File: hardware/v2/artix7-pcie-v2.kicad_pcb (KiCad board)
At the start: 4 copper layers, 60 x 51 mm, 187 parts, among them J1 Conn_02x20_Odd_Even, J10 USB_B_Micro, J2 Conn_02x20_Odd_Even, J4 USB3_A, J5 USB3_A_AS_PCIE, J6 JTAG, J7 Conn_01x02, J8 SER, SW1 PROG, SW2 USER, U1 XC7A75T-FGG484, U10 TPS74701DRCR, U2 MX25L51245GZ2I-10G, U3 TLV62569DBVR, U4 5P49V6965A000NLGI, U5 TLV62569PDDCR, U6 TLV62569DBVR, U7 TLV62569DBVR, U8 TLV62569DBVR, U9 TPS74701DRCR, X1 25MHz/10pF

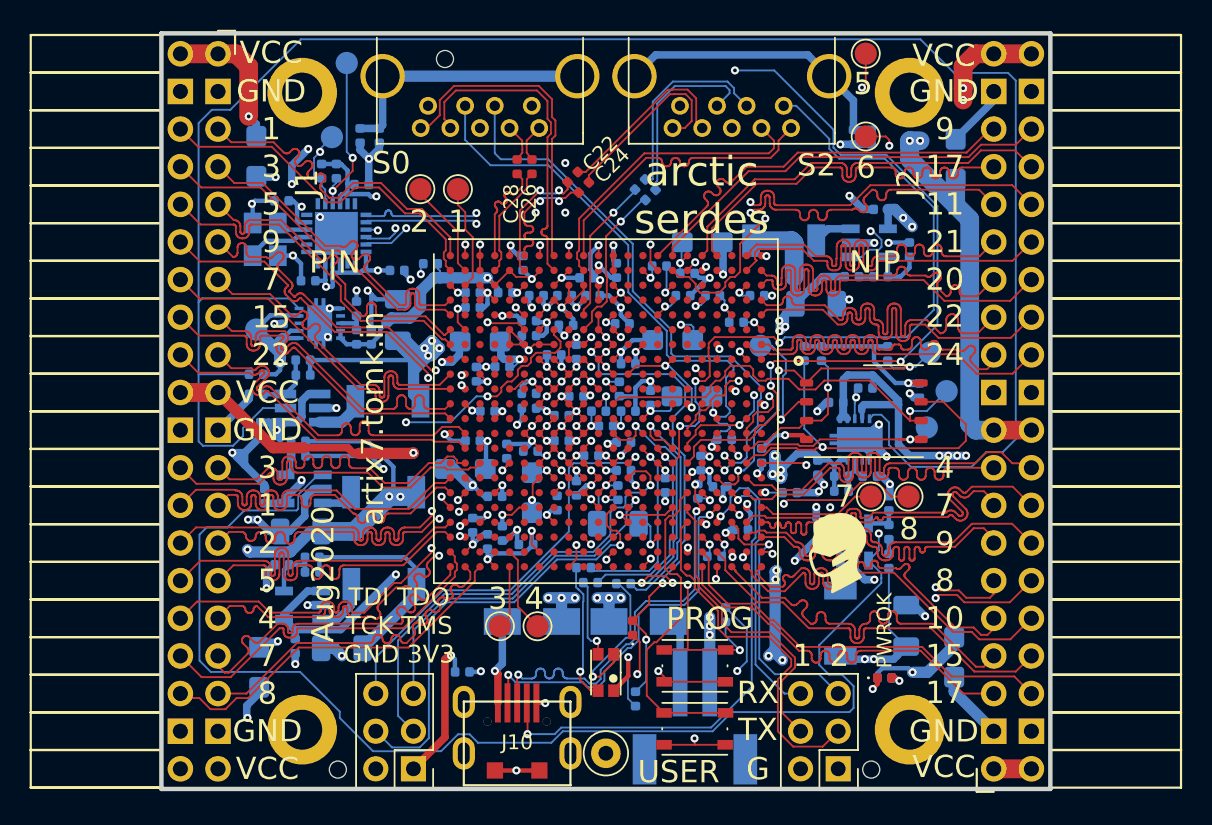
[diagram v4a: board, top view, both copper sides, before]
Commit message: v2 hardware updates: fixed inductor footprint, updates for DFA
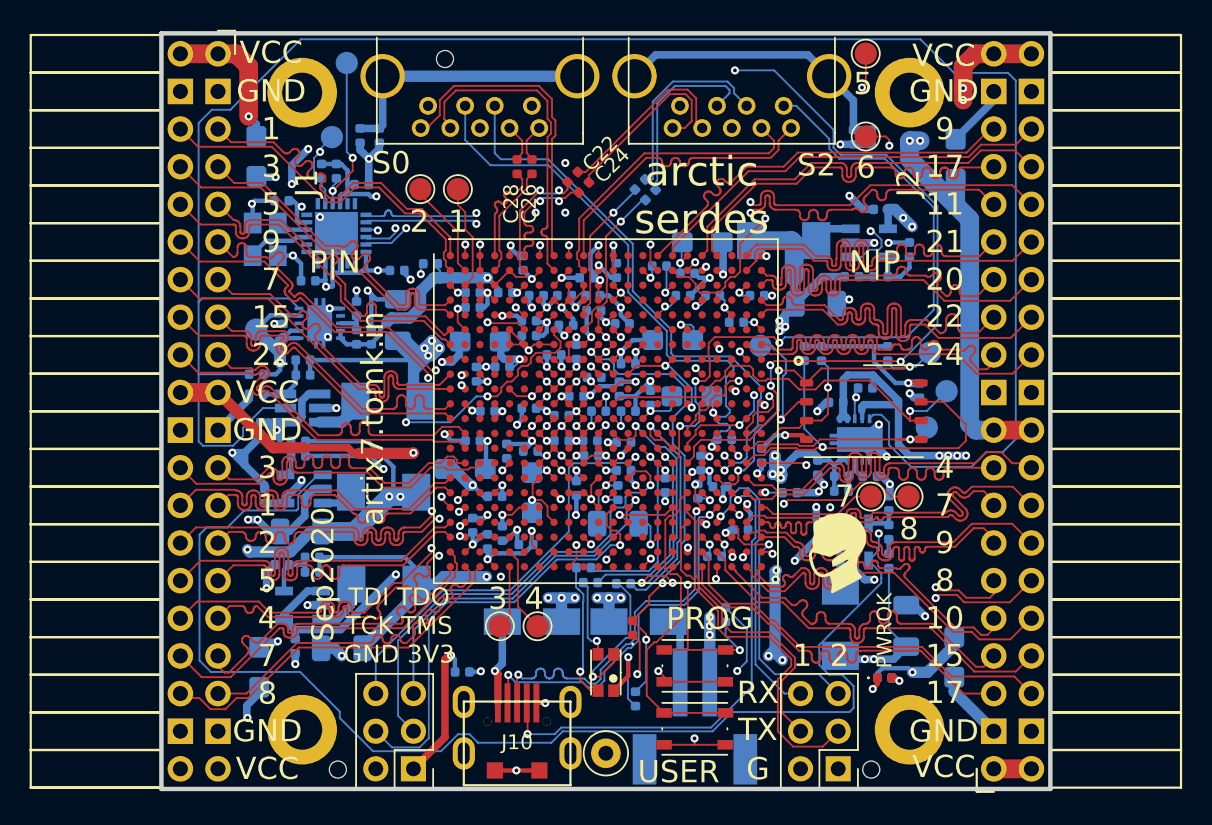
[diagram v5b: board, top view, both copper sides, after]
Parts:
- moved C54 7.83 mm to (140.3, 80.0)
- moved C43 4.76 mm to (140.0, 88.8), turned to 180 degrees
- moved C49 4.53 mm to (140.3, 84.5)
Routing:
- net /Power/VCCBRAM: track 16.5 -> 45.2 mm, vias 1 -> 5
- net +1V8: track 40.5 -> 43.7 mm
- net GND: track 273.6 -> 275.7 mm, vias 126 -> 124
- net +1V0: track 62.8 -> 61.4 mm, vias 23 -> 21
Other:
- board text added: "Sep2020"
- board text removed: "Aug2020"

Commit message: v2 hardare: progress commit on Sept2020 run
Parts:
- moved D1 17.1 mm to (159.5, 105.4), turned to 0 degrees
- moved D5 0.61 mm to (159.5, 104.3)
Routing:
- net /DONE: track 31.7 -> 57.7 mm
- net GND: track 275.7 -> 277.9 mm, vias 124 -> 123
- net Net-(D5-Pad2): track 1.19 -> 2.04 mm
